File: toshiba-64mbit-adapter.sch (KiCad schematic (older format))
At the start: 9 parts, among them U1 TC5364205, U2 S29*L, U3 74HCT244, U4 74HCT244, U5 74HCT244, U6 74HCT244, U7 74HCT244, U8 TPS73633DBV

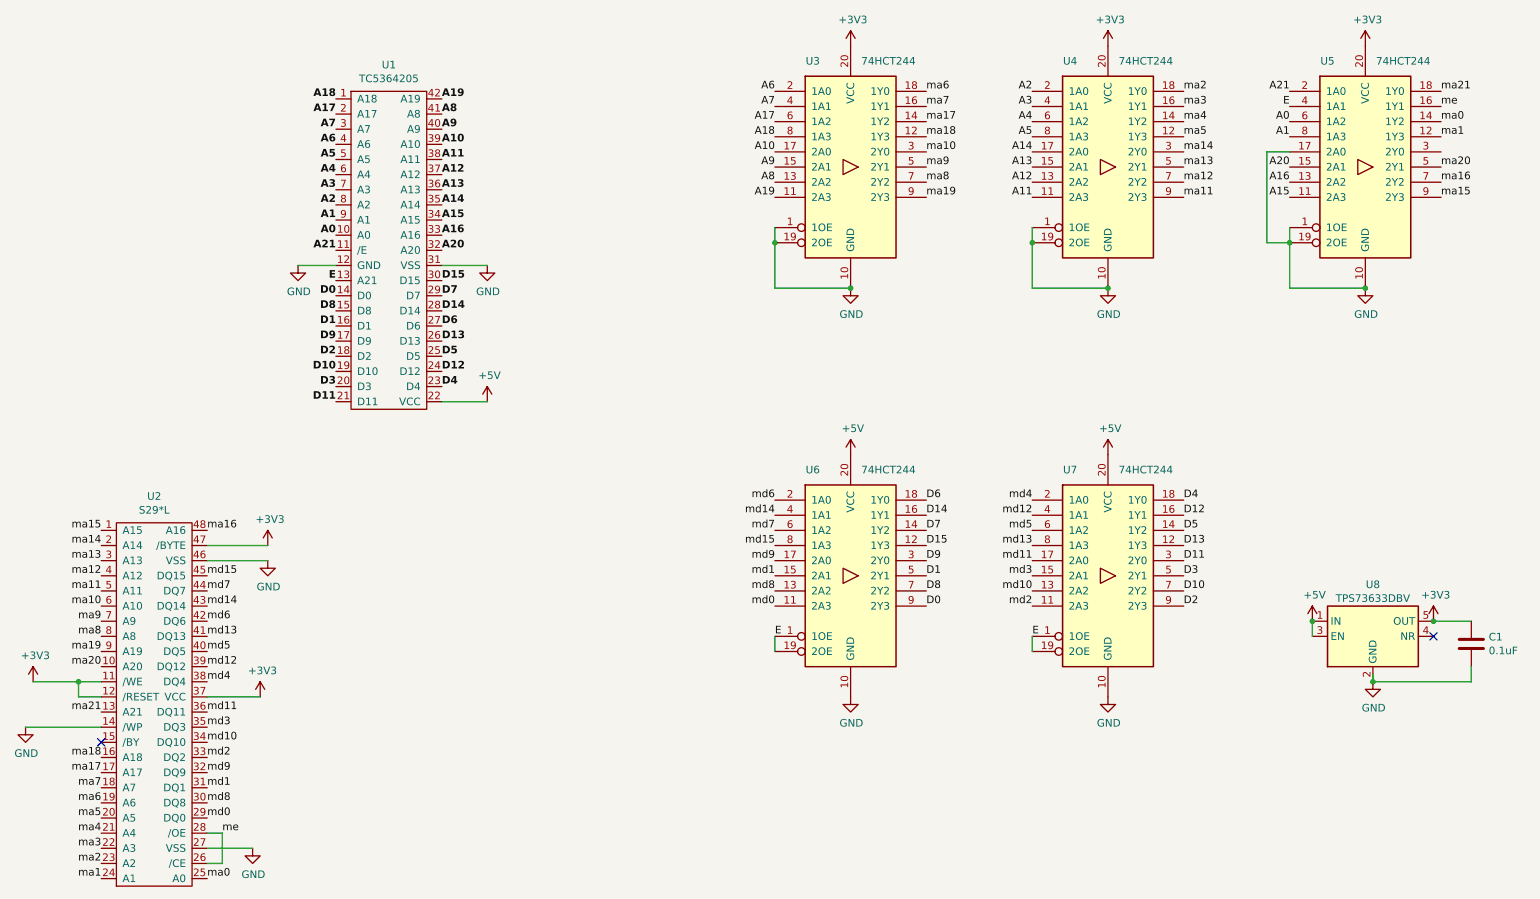
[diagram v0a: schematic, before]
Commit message: Fixed part references
- Changed some HCT parts to LVC
- Moved some labels around a hair
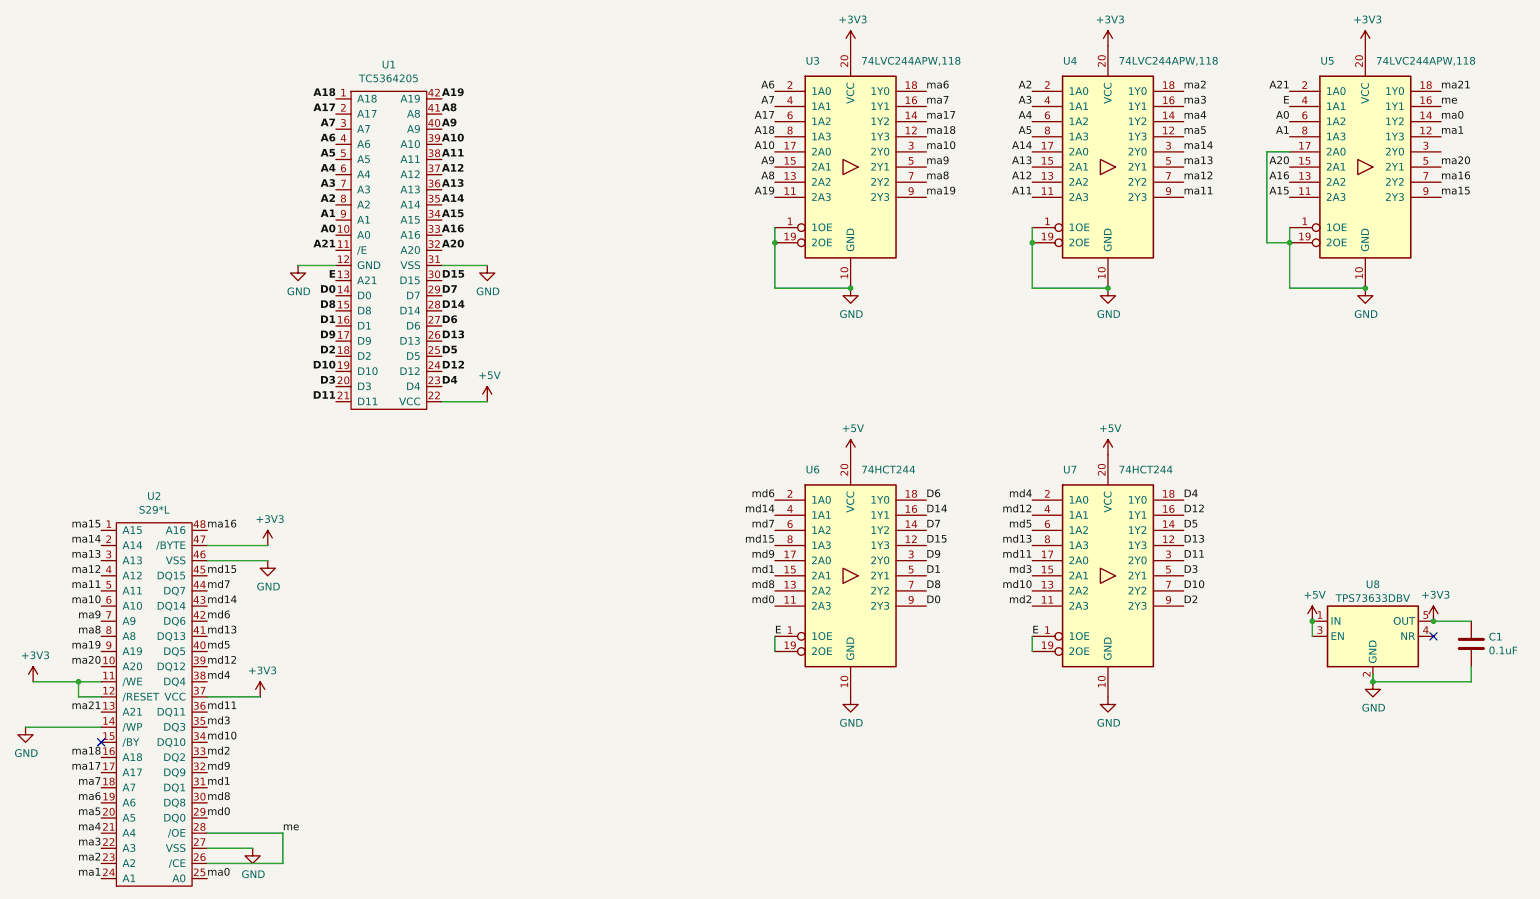
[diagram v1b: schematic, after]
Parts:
- U3, U4, U5: value 74HCT244 -> 74LVC244APW,118
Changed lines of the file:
@@
 	2650 2600 2900 2600
-$Comp
-L toshiba-64mbit-adapter-rescue:74HCT244-74xx U4
-U 1 1 5C861A2E
-P 8000 1950
-F 0 "U4" H 7750 2650 50  0000 C CNN
-F 1 "74HCT244" H 8250 2650 50  0000 C CNN
-F 2 "Package_SO:TSSOP-20_4.4x6.5mm_P0.65mm" H 8000 1950 50  0001 C CNN
-F 3 "https://assets.nexperia.com/documents/data-sheet/74HC_HCT244.pdf" H 8000 1950 50  0001 C CNN
-	1    8000 1950
-	1    0    0    -1
-$EndComp
-$Comp
-L toshiba-64mbit-adapter-rescue:74HCT244-74xx U5
-U 1 1 5C8634EA
-P 9700 1950
-F 0 "U5" H 9450 2650 50  0000 C CNN
-F 1 "74HCT244" H 9950 2650 50  0000 C CNN
-F 2 "Package_SO:TSSOP-20_4.4x6.5mm_P0.65mm" H 9700 1950 50  0001 C CNN
-F 3 "https://assets.nexperia.com/documents/data-sheet/74HC_HCT244.pdf" H 9700 1950 50  0001 C CNN
-	1    9700 1950
-	1    0    0    -1
-$EndComp
 $Comp
 L toshiba-64mbit-adapter-rescue:74HCT244-74xx U7
@@
 Text Label 2050 6250 0    50   ~ 0
 md0
-Text Label 2150 6350 0    50   ~ 0
+Text Label 2550 6350 0    50   ~ 0
 me
 Wire Wire Line
-	2050 6350 2150 6350
-Wire Wire Line
-	2150 6350 2150 6550
-Wire Wire Line
-	2150 6550 2050 6550
+	2050 6350 2550 6350
+Wire Wire Line
+	2550 6350 2550 6550
+Wire Wire Line
+	2550 6550 2050 6550
 Text Label 2050 6650 0    50   ~ 0
 ma0
@@
 $EndComp
 $Comp
-L toshiba-64mbit-adapter-rescue:74HCT244-74xx U3
-U 1 1 5C865388
-P 6300 1950
-F 0 "U3" H 6050 2650 50  0000 C CNN
-F 1 "74HCT244" H 6550 2650 50  0000 C CNN
-F 2 "Package_SO:TSSOP-20_4.4x6.5mm_P0.65mm" H 6300 1950 50  0001 C CNN
-F 3 "https://assets.nexperia.com/documents/data-sheet/74HC_HCT244.pdf" H 6300 1950 50  0001 C CNN
-	1    6300 1950
-	1    0    0    -1
-$EndComp
-$Comp
 L power:+5V #PWR?
 U 1 1 5F8F7548
@@
 	1    0    0    -1
 $EndComp
+$Comp
+L toshiba-64mbit-adapter-rescue:74HCT244-74xx U5
+U 1 1 5C8634EA
+P 9700 1950
+F 0 "U5" H 9450 2650 50  0000 C CNN
+F 1 "74LVC244APW,118" H 10100 2650 50  0000 C CNN
+F 2 "Package_SO:TSSOP-20_4.4x6.5mm_P0.65mm" H 9700 1950 50  0001 C CNN
+F 3 "https://assets.nexperia.com/documents/data-sheet/74LVC_LVCH244A.pdf" H 9700 1950 50  0001 C CNN
+	1    9700 1950
+	1    0    0    -1
+$EndComp
+$Comp
+L toshiba-64mbit-adapter-rescue:74HCT244-74xx U4
+U 1 1 5C861A2E
+P 8000 1950
+F 0 "U4" H 7750 2650 50  0000 C CNN
+F 1 "74LVC244APW,118" H 8400 2650 50  0000 C CNN
+F 2 "Package_SO:TSSOP-20_4.4x6.5mm_P0.65mm" H 8000 1950 50  0001 C CNN
+F 3 "https://assets.nexperia.com/documents/data-sheet/74LVC_LVCH244A.pdf" H 8000 1950 50  0001 C CNN
+	1    8000 1950
+	1    0    0    -1
+$EndComp
+$Comp
+L toshiba-64mbit-adapter-rescue:74HCT244-74xx U3
+U 1 1 5C865388
+P 6300 1950
+F 0 "U3" H 6050 2650 50  0000 C CNN
+F 1 "74LVC244APW,118" H 6700 2650 50  0000 C CNN
+F 2 "Package_SO:TSSOP-20_4.4x6.5mm_P0.65mm" H 6300 1950 50  0001 C CNN
+F 3 "https://assets.nexperia.com/documents/data-sheet/74LVC_LVCH244A.pdf" H 6300 1950 50  0001 C CNN
+	1    6300 1950
+	1    0    0    -1
+$EndComp

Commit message: Added solder jumpers
- Added solder jumpers for configuring / routing byte/word mode
- Added footprints for solder jumpers
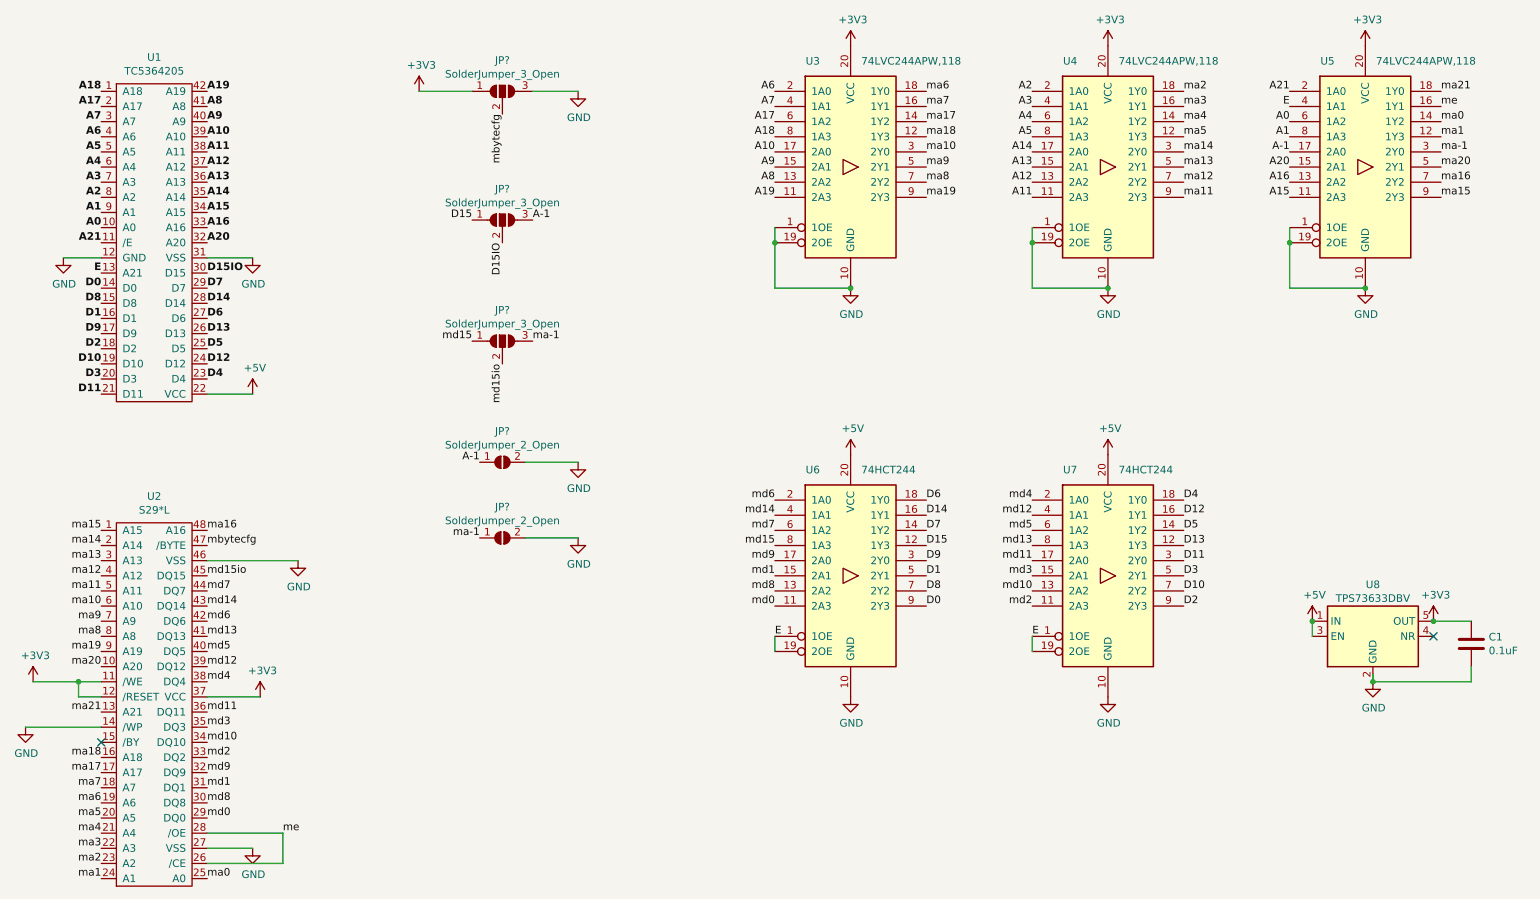
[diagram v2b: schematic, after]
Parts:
- added JP? (x3): SolderJumper_3_Open, Jumper:SolderJumper-3_P2.0mm_Open_TrianglePad1.0x1.5mm_NumberLabels, symbol Jumper:SolderJumper_3_Open
- added JP? (x2): SolderJumper_2_Open, Jumper:SolderJumper-2_P1.3mm_Open_TrianglePad1.0x1.5mm, symbol Jumper:SolderJumper_2_Open
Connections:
- net +3V3: now also JP?.1 (A); no longer U2.47 (/BYTE)
- net D15: now also JP?.1 (A); no longer U1.30 (D15)
- net GND: now also JP?.2 (B), JP?.2 (B), JP?.3 (B); no longer U5.17 (2A0)
- net md15: now also JP?.1 (A); no longer U2.45 (DQ15)
- net ma-1: now reaches U5.3 (2Y0)
- net ma-1: now also JP?.1 (A), JP?.3 (B)
- new net A-1: JP?.1 (A), JP?.3 (B), U5.17 (2A0)
- new net D15IO: JP?.2 (C), U1.30 (D15)
- new net mbytecfg: JP?.2 (C), U2.47 (/BYTE)
- new net md15io: JP?.2 (C), U2.45 (DQ15)
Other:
- moved on the sheet: U1
